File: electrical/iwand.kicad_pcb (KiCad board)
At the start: 2 copper layers, 75.9 x 22 mm, 17 parts, among them J1 GY-33 (GND DR CT VCC), J2 Speaker 8R, J3 Wake button SW1, J4 LiPo 3.7V (+ -), J5 XIAO BAT+ BAT- link, Q1 AO3400, Q2 AO3400, SW2 Power, U1 XIAO ESP32-S3, U3 DFPlayer Mini

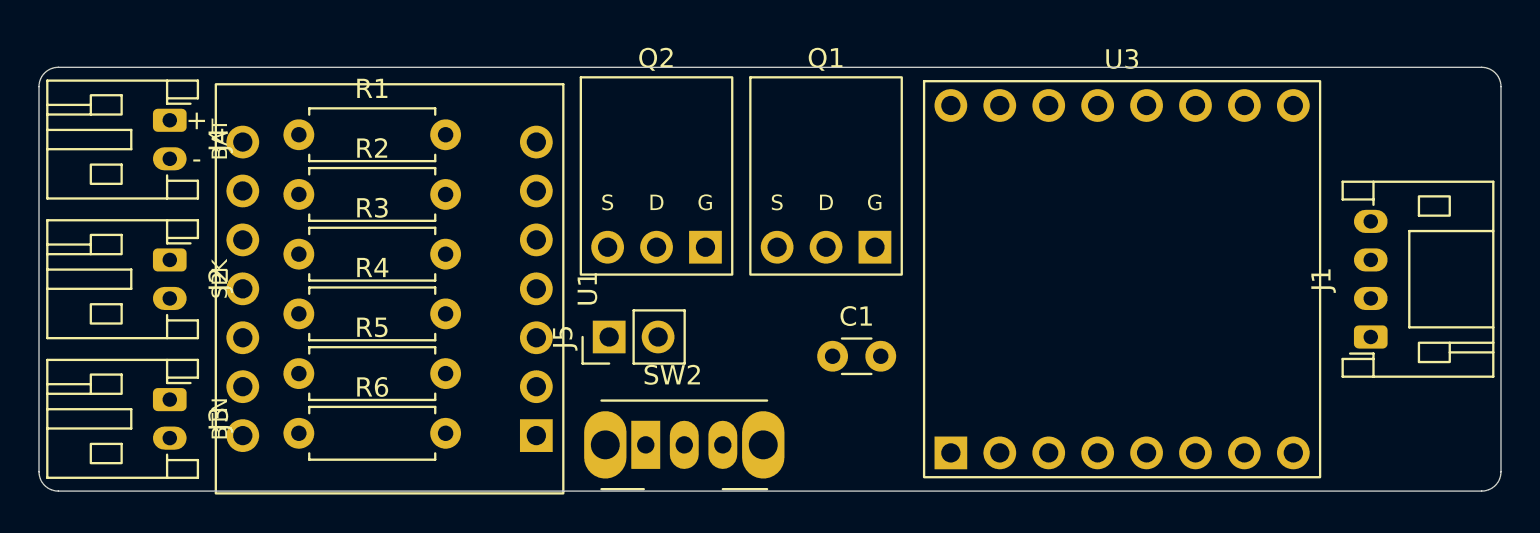
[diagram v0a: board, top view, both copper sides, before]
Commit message: Route the PCB and add fabrication outputs
- Route every net on 2 layers: 0.25 mm signals, and 0.5 mm for the Power
  net class (VBAT, BAT_IN, GND, speaker and the switched grounds).
  Branches to R5/R6/C1 and the gate resistors stay 0.25 mm.
- Shrink module socket pads to 1.6 mm, so a 0.25 mm track can pass
  between two 2.54 mm-pitch pins.
- GND pours on both layers with 47 stitching vias; min resolved thermal
  spokes set to 1.
- Tidy the silkscreen: part references inside their outlines, function
  labels, board name and URL on the underside.
- DRC with schematic parity: 0 violations, 0 unconnected pads.
- Add fab/iwand-gerbers.zip (Gerbers + Excellon drill) and document the
  routing and fab outputs.

Co-Authored-By: Claude Opus 5.5 <noreply@anthropic.com>
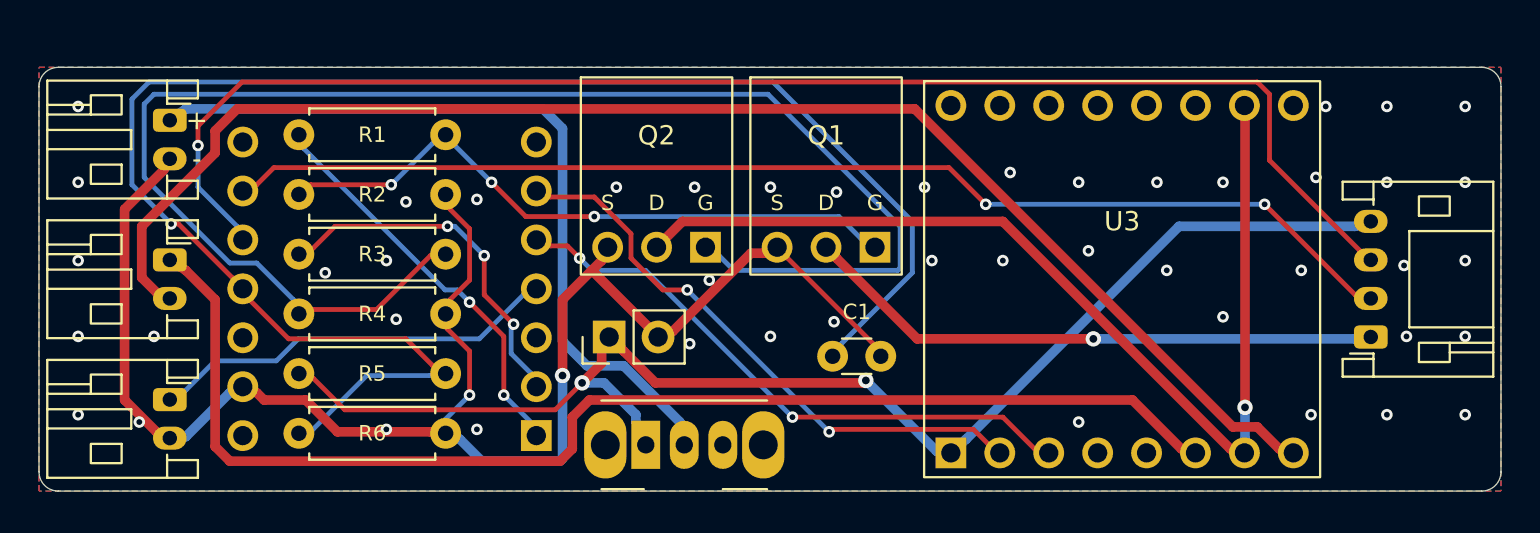
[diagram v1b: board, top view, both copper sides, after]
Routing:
- net /GND: track 0.00 -> 86.3 mm, vias 0 -> 49
- net /VBAT_SENSE: track 0.00 -> 86.2 mm, vias 0 -> 1
- net /Q2_GATE: track 0.00 -> 78.8 mm
- net /SPK2: track 0.00 -> 74.8 mm
- net /GY33_CT: track 0.00 -> 74.5 mm, vias 0 -> 1
- net /VBAT: track 0.00 -> 71.0 mm, vias 0 -> 2
- net /SPK1: track 0.00 -> 65.3 mm
- net /GY33_DR: track 0.00 -> 61.8 mm, vias 0 -> 2
- net /AUDIO_GND: track 0.00 -> 54.0 mm, vias 0 -> 1
- net /BAT_IN: track 0.00 -> 41.1 mm
- net /Q1_GATE: track 0.00 -> 33.5 mm, vias 0 -> 3
- net /UART_RX: track 0.00 -> 31.1 mm, vias 0 -> 2
- net /UART_TX: track 0.00 -> 30.4 mm, vias 0 -> 2
- net /SENSOR_GND: track 0.00 -> 30.3 mm, vias 0 -> 1
- net /D3_BTN: track 0.00 -> 21.3 mm
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- added copper zone on B.Cu, net /GND
- added copper zone on F.Cu, net /GND
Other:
- board text added: "GY-33"
- board text added: "PWR"
- board text added: "XIAO BAT"
- board text added: "github.com/dangwalsh/iwand"
- board text added: "iWand v0.2"

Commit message: Board v0.3: visible J4 polarity marks, JST-PH socket for J5
J4's +/- silkscreen marks sat under the JST housing, so a reversed
battery plug went unnoticed. Move the front marks clear of the housing,
add matching marks on the back beside BAT, and note in the README that
J4 is the reverse of most LiPo plugs.

Replace the J5 pin header (XIAO BAT+/BAT- link) with a JST PH top-entry
socket (B2B-PH-K). It is lower than a header and Dupont plug and takes
the same PHR-2 plug as J1-J4. A side-entry S2B-PH-K doesn't fit between
Q2 and SW2. Re-route the nearby GND and VBAT tracks to the new pads.

Bump the revision to v0.3 and regenerate the Gerbers, drill files and
the populated PCB STEP model.

Co-Authored-By: Claude Opus 5.5 <noreply@anthropic.com>
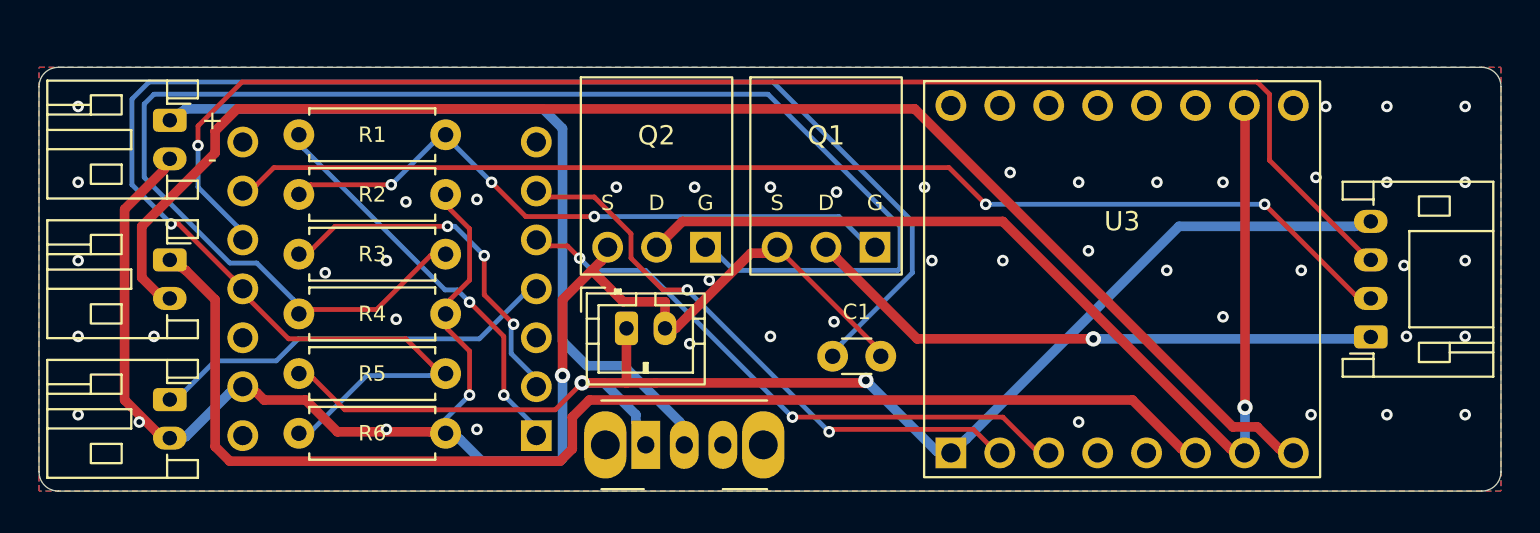
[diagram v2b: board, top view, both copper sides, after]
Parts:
- J5: footprint Connector_PinHeader_2.54mm:PinHeader_1x02_P2.54mm_Vertical -> Connector_JST:JST_PH_B2B-PH-K_1x02_P2.00mm_Vertical
- moved J5 1.01 mm to (130.5, 113.5), turned to 0 degrees
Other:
- board text added: "iWand v0.3"
- board text removed: "iWand v0.2"
